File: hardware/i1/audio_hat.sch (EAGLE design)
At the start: 6 parts

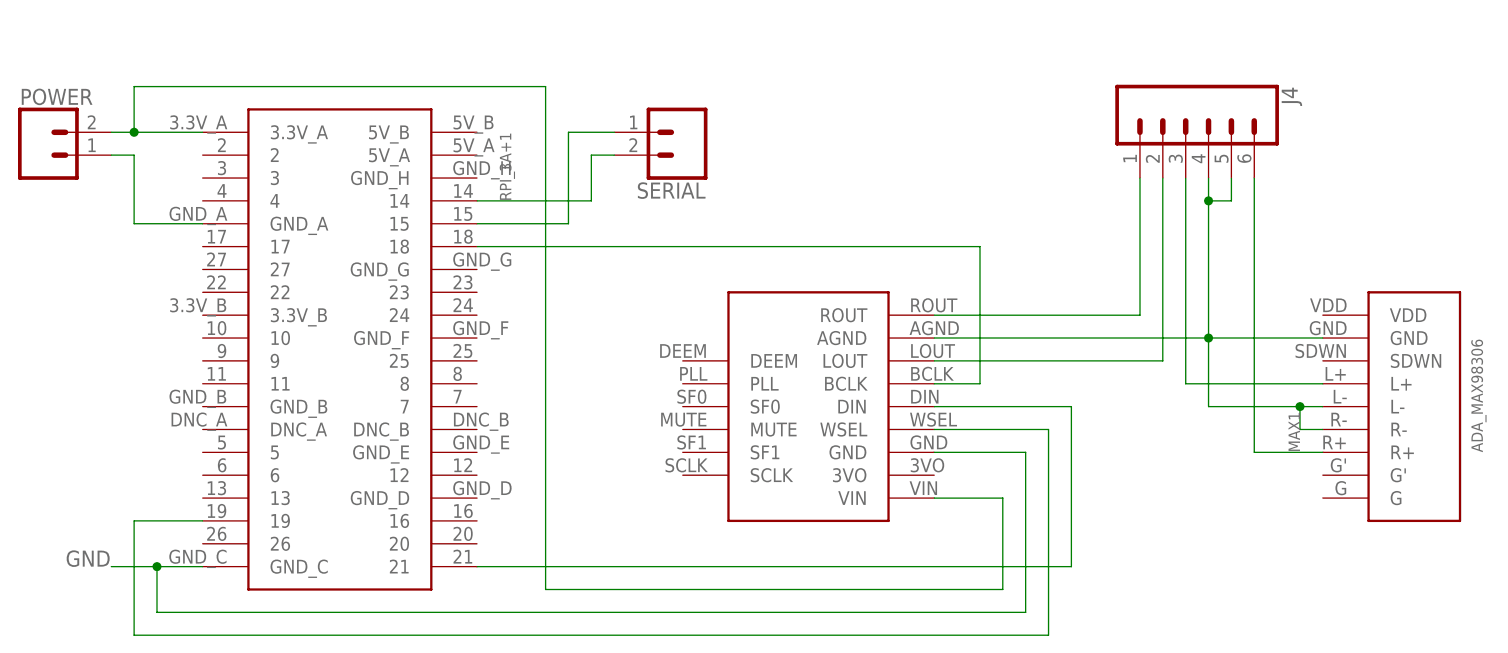
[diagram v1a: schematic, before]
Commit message: Audio hat now makes use of PCB via rivets
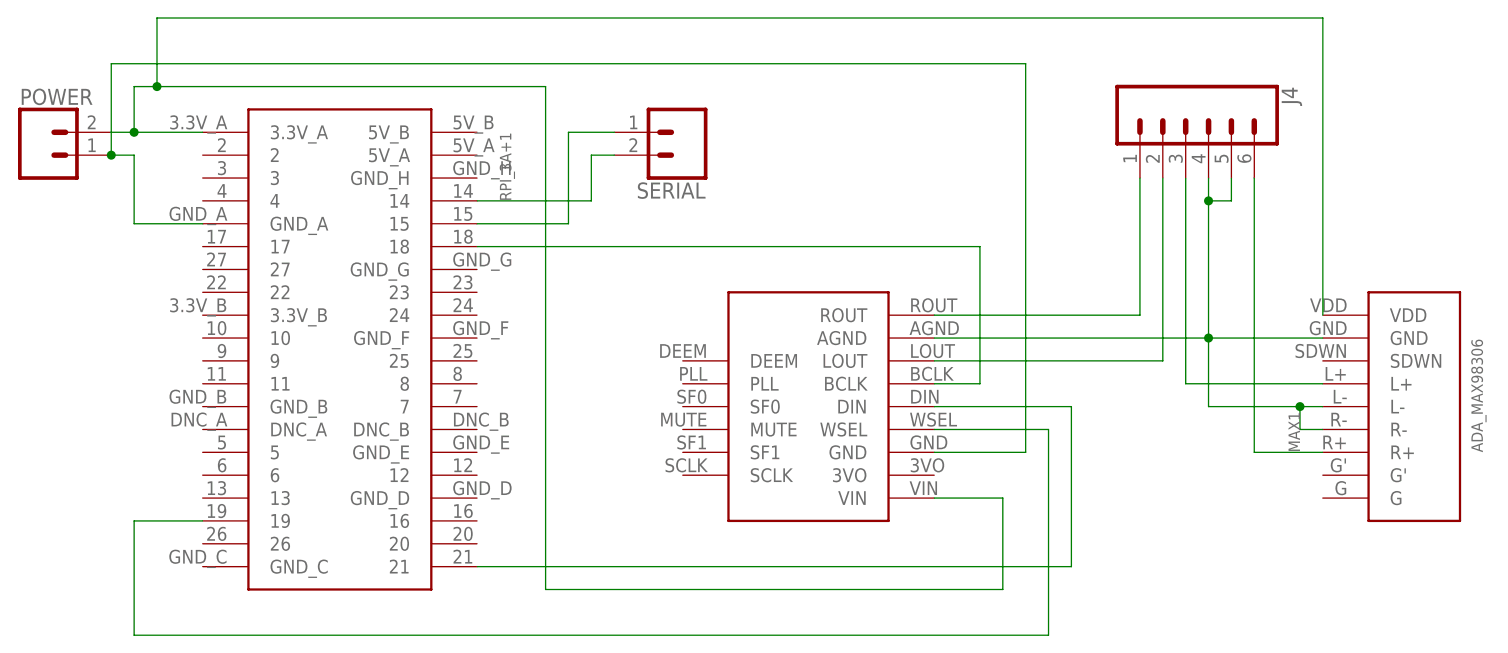
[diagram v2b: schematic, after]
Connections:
- removed net GND: RPI_3A+1.GND_C, UDA1.GND
- net N$2: now also UDA1.GND
- net N$3: now also MAX1.VDD
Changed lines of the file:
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@@
 <wire x1="76.2" y1="48.26" x2="25.4" y2="48.26" width="0.1524" layer="91"/>
 <wire x1="25.4" y1="48.26" x2="25.4" y2="104.14" width="0.1524" layer="91"/>
-<wire x1="25.4" y1="104.14" x2="-20.32" y2="104.14" width="0.1524" layer="91"/>
+<wire x1="25.4" y1="104.14" x2="-17.78" y2="104.14" width="0.1524" layer="91"/>
+<pinref part="RPI_3A+1" gate="G$1" pin="3.3V_A"/>
+<wire x1="-17.78" y1="104.14" x2="-20.32" y2="104.14" width="0.1524" layer="91"/>
 <wire x1="-20.32" y1="104.14" x2="-20.32" y2="99.06" width="0.1524" layer="91"/>
-<pinref part="RPI_3A+1" gate="G$1" pin="3.3V_A"/>
 <wire x1="-20.32" y1="99.06" x2="-12.7" y2="99.06" width="0.1524" layer="91"/>
 <pinref part="POWER" gate="G$1" pin="2"/>
 <wire x1="-22.86" y1="99.06" x2="-20.32" y2="99.06" width="0.1524" layer="91"/>
 <junction x="-20.32" y="99.06"/>
+<pinref part="MAX1" gate="G$1" pin="VDD"/>
+<wire x1="111.76" y1="78.74" x2="111.76" y2="111.76" width="0.1524" layer="91"/>
+<wire x1="111.76" y1="111.76" x2="-17.78" y2="111.76" width="0.1524" layer="91"/>
+<wire x1="-17.78" y1="111.76" x2="-17.78" y2="104.14" width="0.1524" layer="91"/>
+<junction x="-17.78" y="104.14"/>
 </segment>
 </net>
@@
 </segment>
 </net>
-<net name="GND" class="0">
-<segment>
-<wire x1="-17.78" y1="45.72" x2="78.74" y2="45.72" width="0.1524" layer="91"/>
-<wire x1="78.74" y1="45.72" x2="78.74" y2="63.5" width="0.1524" layer="91"/>
-<pinref part="UDA1" gate="G$1" pin="GND"/>
-<wire x1="78.74" y1="63.5" x2="68.58" y2="63.5" width="0.1524" layer="91"/>
-<wire x1="-17.78" y1="45.72" x2="-17.78" y2="50.8" width="0.1524" layer="91"/>
-<pinref part="RPI_3A+1" gate="G$1" pin="GND_C"/>
-<wire x1="-17.78" y1="50.8" x2="-12.7" y2="50.8" width="0.1524" layer="91"/>
-<wire x1="-17.78" y1="50.8" x2="-22.86" y2="50.8" width="0.1524" layer="91"/>
-<junction x="-17.78" y="50.8"/>
-<label x="-27.94" y="50.8" size="1.778" layer="95"/>
-</segment>
-</net>
 <net name="N$2" class="0">
 <segment>
@@
 <pinref part="RPI_3A+1" gate="G$1" pin="GND_A"/>
 <wire x1="-20.32" y1="88.9" x2="-12.7" y2="88.9" width="0.1524" layer="91"/>
+<pinref part="UDA1" gate="G$1" pin="GND"/>
+<wire x1="68.58" y1="63.5" x2="78.74" y2="63.5" width="0.1524" layer="91"/>
+<wire x1="78.74" y1="63.5" x2="78.74" y2="106.68" width="0.1524" layer="91"/>
+<wire x1="78.74" y1="106.68" x2="-22.86" y2="106.68" width="0.1524" layer="91"/>
+<wire x1="-22.86" y1="106.68" x2="-22.86" y2="96.52" width="0.1524" layer="91"/>
+<junction x="-22.86" y="96.52"/>
 </segment>
 </net>
